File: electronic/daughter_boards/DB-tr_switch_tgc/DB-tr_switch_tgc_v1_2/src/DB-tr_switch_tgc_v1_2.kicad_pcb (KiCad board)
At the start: 2 copper layers, 45.7 x 52.1 mm, 38 parts, among them P1 SMA, P2 CONN_01X19, P3 CONN_01X02, SW1 SWITCH_INV, T1 TRANSFO_6pins, U1 MD0100, U2 AD8331

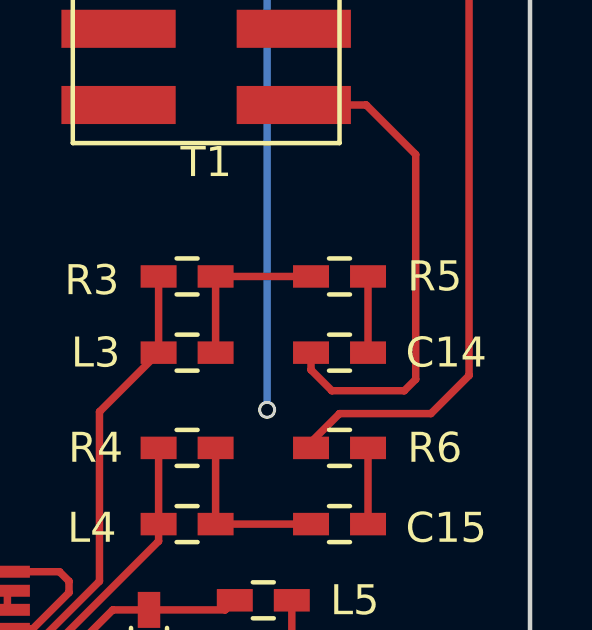
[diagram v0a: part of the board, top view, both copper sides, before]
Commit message: adding motor_control_v3 and trs_tgc_v2
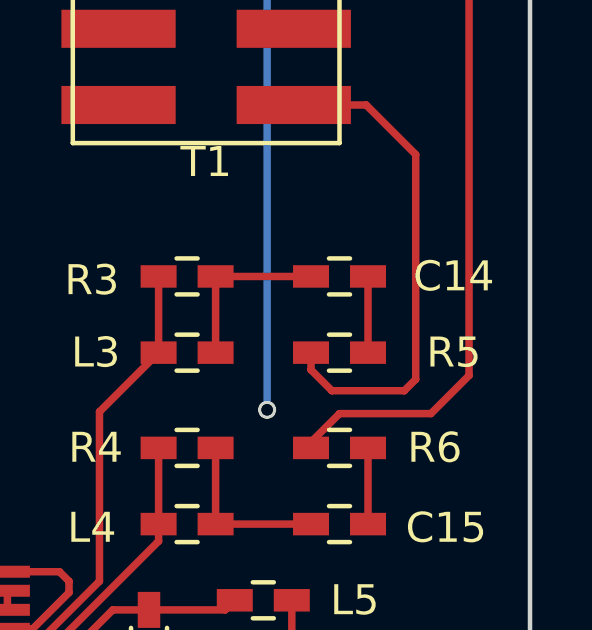
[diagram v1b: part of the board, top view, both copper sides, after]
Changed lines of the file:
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@@
   (layers
     (0 F.Cu signal)
-    (31 B.Cu signal)
+    (31 B.Cu signal hide)
     (32 B.Adhes user)
     (33 F.Adhes user)
@@
     (tags "capacitor 0603")
     (attr smd)
-    (fp_text reference C14 (at -3.556 -2.54 180) (layer F.SilkS)
+    (fp_text reference C14 (at -3.81 0 180) (layer F.SilkS)
       (effects (font (size 1 1) (thickness 0.15)))
     )
@@
     (tags "capacitor 0603")
     (attr smd)
-    (fp_text reference R5 (at 3.175 -2.54) (layer F.SilkS)
-      (effects (font (size 1 1) (thickness 0.15)))
-    )
+    (fp_text reference R5 (at 3.81 0) (layer F.SilkS)
+      (effects (font (size 1 1) (thickness 0.15)))
+    )
